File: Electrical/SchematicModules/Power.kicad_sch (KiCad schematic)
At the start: 5 parts

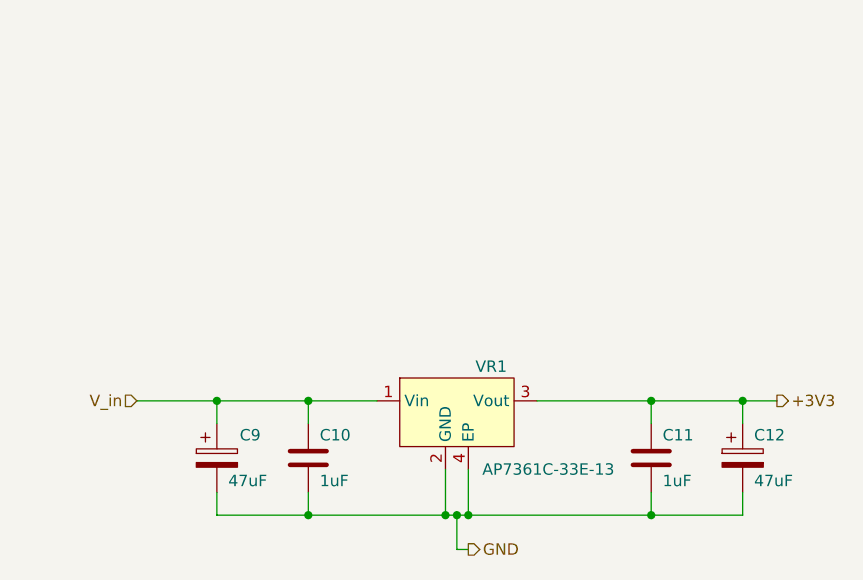
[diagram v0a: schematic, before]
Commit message: Added layout for prototype 1
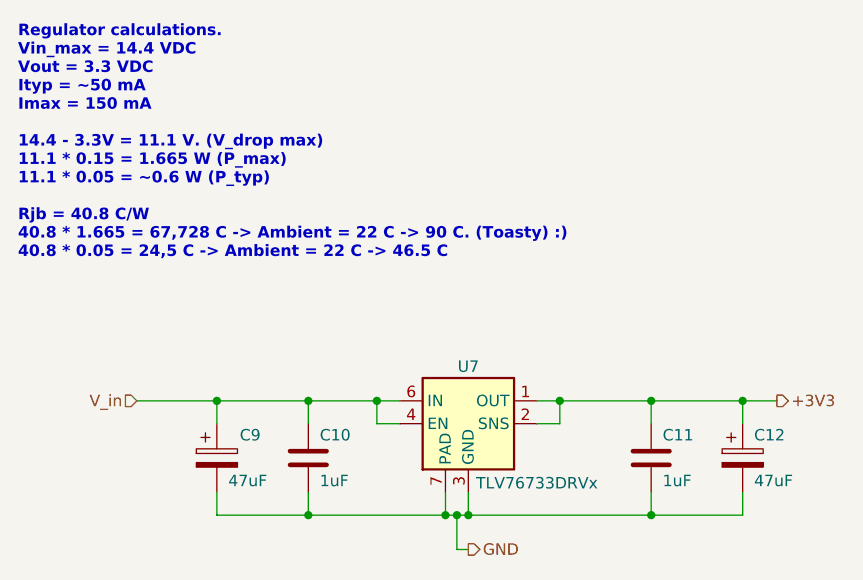
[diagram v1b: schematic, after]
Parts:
- removed VR1: AP7361C-33E-13, Package_TO_SOT_SMD:SOT-223, symbol NyaCentralenheten:Voltage_Regulator
- added U7: TLV76733DRVx, Package_SON:WSON-6-1EP_2x2mm_P0.65mm_EP1x1.6mm_ThermalVias, symbol Regulator_Linear:TLV76733DRVx
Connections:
- net +3V3: now also U7.1 (OUT), U7.2 (SNS)
- net GND: now also U7.3 (GND), U7.5 (GND), U7.7 (PAD)
- net V_in: now also U7.4 (EN), U7.6 (IN)
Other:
- note added: "Regulator calculations. Vin_max = 14.4 VDC Vout = 3.3 VDC Ityp = ~50 mA Imax = 150 mA 14.4 - 3.3V = 11.1 V. (V_drop max) 11.1 * 0.15 = 1.665 W (P_max) 11.1 * 0.05 = ~0.6 W (P_typ) Rjb = 40.8 C/W 40.8 * 1.665 = 67,728 C -> Ambient = 22 C -> 90 C. (Toasty) :) 40.8 * 0.05 = 24,5 C -> Ambient = 22 C -> 46.5 C"
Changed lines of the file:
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@@
 	(paper "A4")
 	(junction
+		(at 147.32 95.25)
+		(diameter 0)
+		(color 0 0 0 0)
+	)
+	(junction
 		(at 157.48 107.95)
 		(diameter 0)
@@
 	)
 	(junction
+		(at 167.64 95.25)
+		(diameter 0)
+		(color 0 0 0 0)
+	)
+	(junction
 		(at 177.8 107.95)
 		(diameter 0)
@@
 	(wire
 		(pts
-			(xy 165.1 95.25) (xy 177.8 95.25)
-		)
-		(stroke
-			(width 0)
-			(type default)
-		)
-	)
-	(wire
-		(pts
-			(xy 154.94 102.87) (xy 154.94 107.95)
-		)
-		(stroke
-			(width 0)
-			(type default)
-		)
-	)
-	(wire
-		(pts
-			(xy 157.48 102.87) (xy 157.48 107.95)
+			(xy 165.1 95.25) (xy 167.64 95.25)
+		)
+		(stroke
+			(width 0)
+			(type default)
+		)
+	)
+	(wire
+		(pts
+			(xy 167.64 97.79) (xy 167.64 95.25)
+		)
+		(stroke
+			(width 0)
+			(type default)
+		)
+	)
+	(wire
+		(pts
+			(xy 157.48 105.41) (xy 157.48 107.95)
+		)
+		(stroke
+			(width 0)
+			(type default)
+		)
+	)
+	(wire
+		(pts
+			(xy 165.1 97.79) (xy 167.64 97.79)
 		)
 		(stroke
@@
 	(wire
 		(pts
+			(xy 147.32 97.79) (xy 147.32 95.25)
+		)
+		(stroke
+			(width 0)
+			(type default)
+		)
+	)
+	(wire
+		(pts
 			(xy 177.8 107.95) (xy 177.8 105.41)
 		)
@@
 	(wire
 		(pts
+			(xy 167.64 95.25) (xy 177.8 95.25)
+		)
+		(stroke
+			(width 0)
+			(type default)
+		)
+	)
+	(wire
+		(pts
 			(xy 187.96 95.25) (xy 177.8 95.25)
 		)
@@
 	(wire
 		(pts
+			(xy 154.94 105.41) (xy 154.94 107.95)
+		)
+		(stroke
+			(width 0)
+			(type default)
+		)
+	)
+	(wire
+		(pts
+			(xy 147.32 95.25) (xy 149.86 95.25)
+		)
+		(stroke
+			(width 0)
+			(type default)
+		)
+	)
+	(wire
+		(pts
 			(xy 156.21 111.76) (xy 157.48 111.76)
 		)
@@
 	(wire
 		(pts
+			(xy 149.86 97.79) (xy 147.32 97.79)
+		)
+		(stroke
+			(width 0)
+			(type default)
+		)
+	)
+	(wire
+		(pts
 			(xy 129.54 105.41) (xy 129.54 107.95)
 		)
@@
 			(width 0)
 			(type default)
+		)
+	)
+	(text "Regulator calculations.\nVin_max = 14.4 VDC\nVout = 3.3 VDC\nItyp = ~50 mA\nImax = 150 mA\n\n14.4 - 3.3V = 11.1 V. (V_drop max)\n11.1 * 0.15 = 1.665 W (P_max)\n11.1 * 0.05 = ~0.6 W (P_typ)\n\nRjb = 40.8 C/W\n40.8 * 1.665 = 67,728 C -> Ambient = 22 C -> 90 C. (Toasty) :)\n40.8 * 0.05 = 24,5 C -> Ambient = 22 C -> 46.5 C\n\n"
+		(exclude_from_sim no)
+		(at 107.442 67.564 0)
+		(effects
+			(font
+				(size 1.27 1.27)
+				(thickness 0.254)
+				(bold yes)
+			)
+			(justify left)
 		)
 	)
@@
 			)
 			(justify left)
+		)
+	)
+	(symbol
+		(lib_id "Regulator_Linear:TLV76733DRVx")
+		(at 157.48 97.79 0)
+		(unit 1)
+		(exclude_from_sim no)
+		(in_bom yes)
+		(on_board yes)
+		(dnp no)
+		(property "Reference" "U7"
+			(at 157.48 91.44 0)
+			(effects
+				(font
+					(size 1.27 1.27)
+				)
+			)
+		)
+		(property "Value" "TLV76733DRVx"
+			(at 165.1 104.394 0)
+			(effects
+				(font
+					(size 1.27 1.27)
+				)
+			)
+		)
+		(property "Footprint" "Package_SON:WSON-6-1EP_2x2mm_P0.65mm_EP1x1.6mm_ThermalVias"
+			(at 157.48 86.36 0)
+			(effects
+				(font
+					(size 1.27 1.27)
+				)
+				(hide yes)
+			)
+		)
+		(property "Datasheet" "www.ti.com/lit/gpn/TLV767"
+			(at 156.21 97.79 0)
+			(effects
+				(font
+					(size 1.27 1.27)
+				)
+				(hide yes)
+			)
+		)
+		(property "Description" "1A Precision Linear Voltage Regulator, with enable pin, Fixed Output 3.3V, WSON6"
+			(at 157.48 97.79 0)
+			(effects
+				(font
+					(size 1.27 1.27)
+				)
+				(hide yes)
+			)
+		)
+		(pin "2"
+		)
+		(pin "3"
+		)
+		(pin "4"
+		)
+		(pin "5"
+		)
+		(pin "6"
+		)
+		(pin "7"
+		)
+		(pin "1"
+		)
+		(instances
+			(project ""
+				(path "/3890375c-1dd0-4d9e-918b-5385f86ea973/97fff623-042a-4167-bc14-3239946f08aa"
+					(reference "U7")
+					(unit 1)
+				)
+			)
 		)
 	)
@@
 					(unit 1)
 				)
-			)
-		)
-	)
-	(symbol
-		(lib_id "NyaCentralenheten:Voltage_Regulator")
-		(at 156.21 96.52 0)
-		(unit 1)
-		(exclude_from_sim no)
-		(in_bom yes)
-		(on_board yes)
-		(dnp no)
-		(property "Reference" "VR1"
-			(at 160.02 91.44 0)
-			(effects
-				(font
-					(size 1.27 1.27)
-				)
-			)
-		)
-		(property "Value" "AP7361C-33E-13"
-			(at 166.37 102.87 0)
-			(effects
-				(font
-					(size 1.27 1.27)
-				)
-			)
-		)
-		(property "Footprint" "Package_TO_SOT_SMD:SOT-223"
-			(at 157.48 96.52 0)
-			(effects
-				(font
-					(size 1.27 1.27)
-				)
-				(hide yes)
-			)
-		)
-		(property "Datasheet" "https://www.diodes.com/assets/Datasheets/AP7361C.pdf"
-			(at 157.48 96.52 0)
-			(effects
-				(font
-					(size 1.27 1.27)
-				)
-				(hide yes)
-			)
-		)
-		(property "Description" ""
-			(at 156.21 96.52 0)
-			(effects
-				(font
-					(size 1.27 1.27)
-				)
-				(hide yes)
-			)
-		)
-		(pin "1"
-		)
-		(pin "2"
-		)
-		(pin "3"
-		)
-		(pin "4"
-		)
-		(instances
-			(project "AutoTiller"
-				(path "/3890375c-1dd0-4d9e-918b-5385f86ea973/97fff623-042a-4167-bc14-3239946f08aa"
-					(reference "VR1")
-					(unit 1)
-				)

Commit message: Finalizing the layout
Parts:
- C9: now not fitted
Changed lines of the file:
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@@
 		(exclude_from_sim no)
 		(in_bom yes)
-		(on_board yes)
-		(dnp no)
+		(on_board no)
+		(dnp yes)
 		(property "Reference" "C9"
 			(at 132.08 99.06 0)
